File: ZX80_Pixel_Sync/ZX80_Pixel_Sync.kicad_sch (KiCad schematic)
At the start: 7 parts, among them IC202 74LS74, J1 IC201, J2 To_Minstrel2

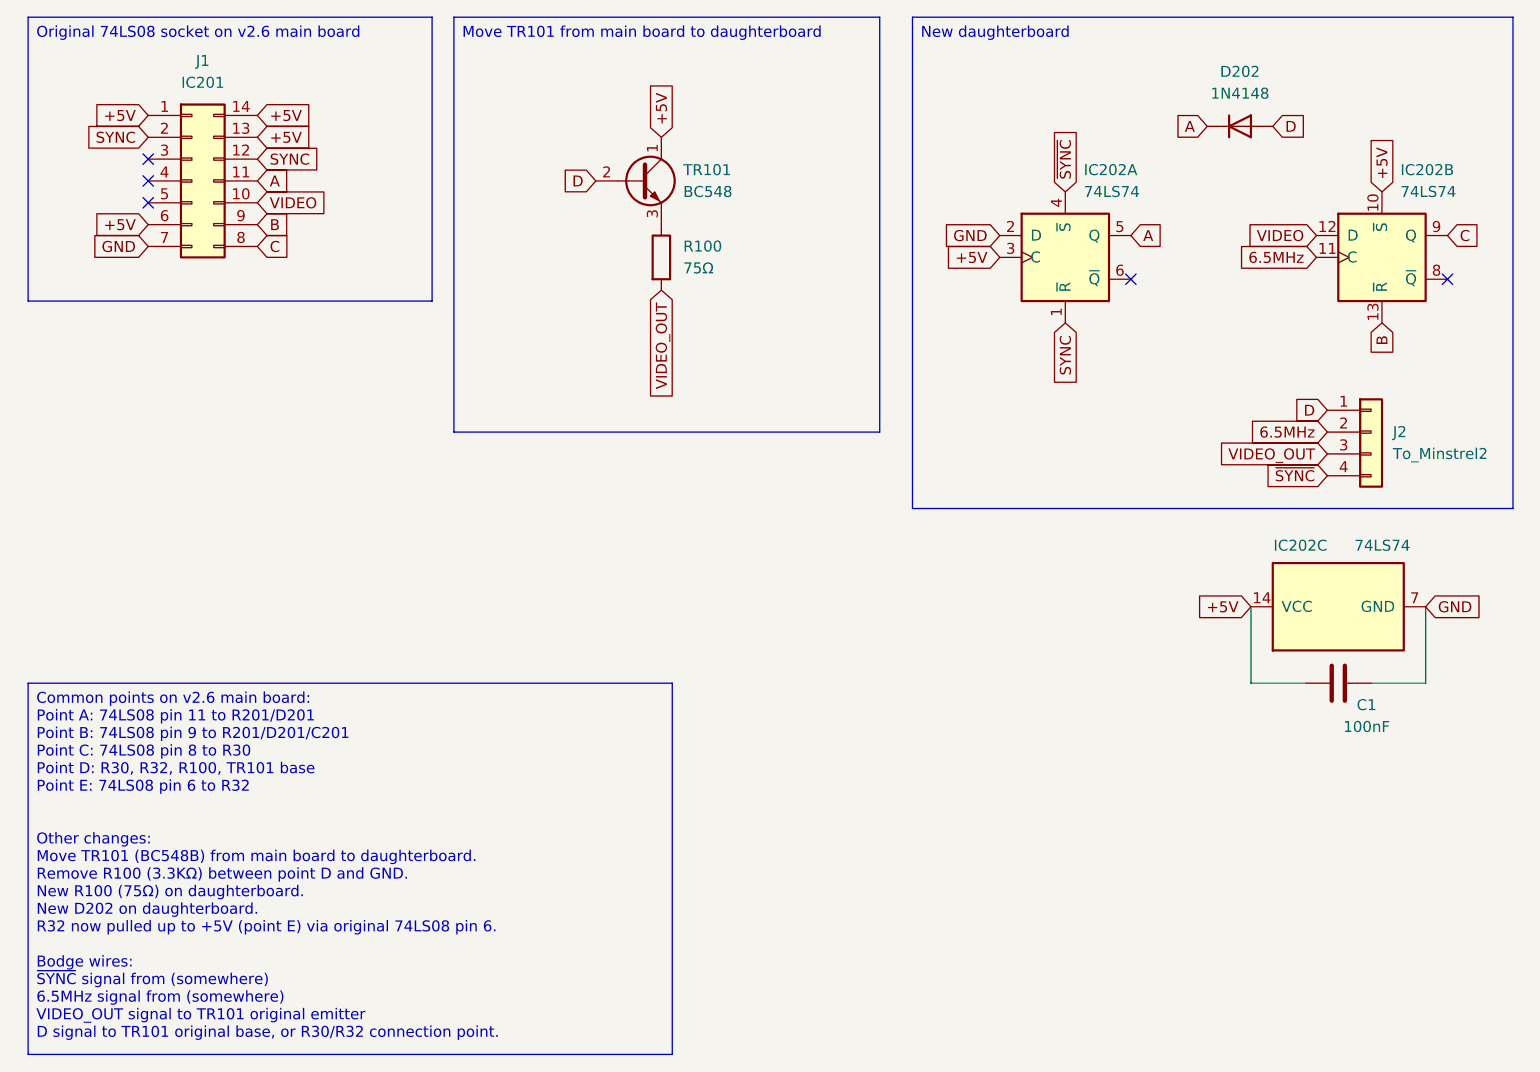
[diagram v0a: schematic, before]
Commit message: Modified PCB layout after testing initial layout
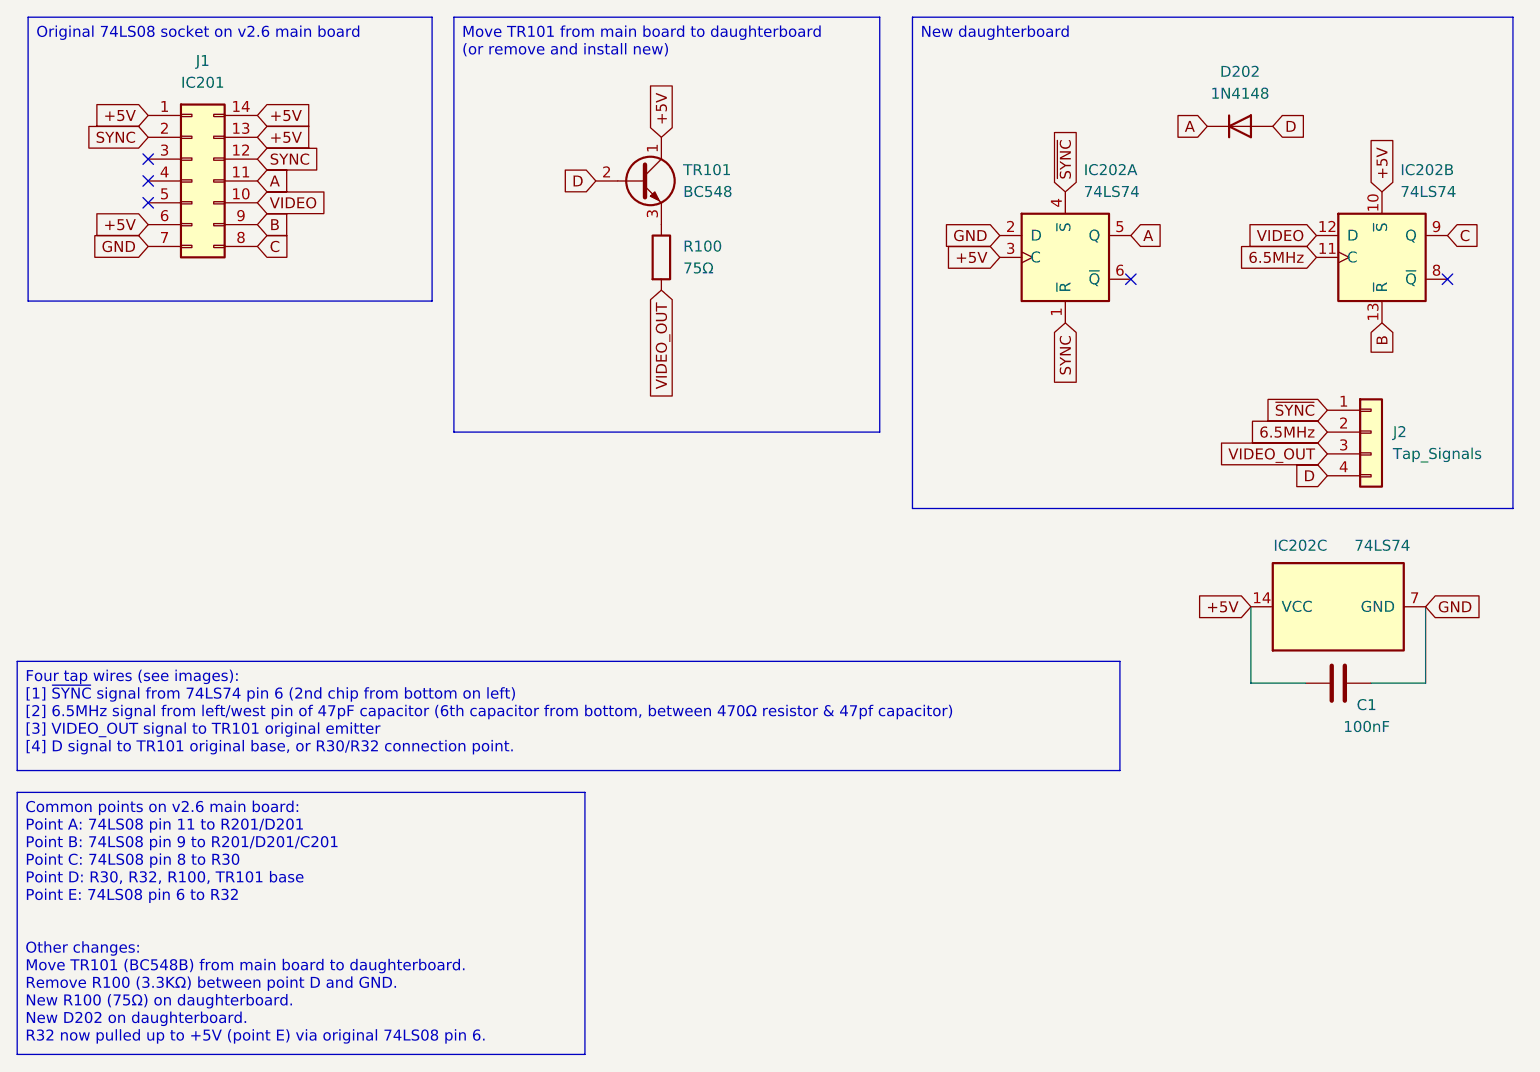
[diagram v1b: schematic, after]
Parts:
- J2: value To_Minstrel2 -> Tap_Signals
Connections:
- net D: now also J2.4 (Pin_4); no longer J2.1 (Pin_1)
- net ~{SYNC}: now also J2.1 (Pin_1); no longer J2.4 (Pin_4)
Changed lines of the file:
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@@
 		)
 	)
-	(text_box "Common points on v2.6 main board:\nPoint A: 74LS08 pin 11 to R201/D201\nPoint B: 74LS08 pin 9 to R201/D201/C201\nPoint C: 74LS08 pin 8 to R30\nPoint D: R30, R32, R100, TR101 base\nPoint E: 74LS08 pin 6 to R32\n\n\nOther changes:\nMove TR101 (BC548B) from main board to daughterboard.\nRemove R100 (3.3KΩ) between point D and GND.\nNew R100 (75Ω) on daughterboard.\nNew D202 on daughterboard.\nR32 now pulled up to +5V (point E) via original 74LS08 pin 6.\n\nBodge wires:\n~{SYNC} signal from (somewhere)\n6.5MHz signal from (somewhere)\nVIDEO_OUT signal to TR101 original emitter\nD signal to TR101 original base, or R30/R32 connection point."
+	(text_box "Common points on v2.6 main board:\nPoint A: 74LS08 pin 11 to R201/D201\nPoint B: 74LS08 pin 9 to R201/D201/C201\nPoint C: 74LS08 pin 8 to R30\nPoint D: R30, R32, R100, TR101 base\nPoint E: 74LS08 pin 6 to R32\n\n\nOther changes:\nMove TR101 (BC548B) from main board to daughterboard.\nRemove R100 (3.3KΩ) between point D and GND.\nNew R100 (75Ω) on daughterboard.\nNew D202 on daughterboard.\nR32 now pulled up to +5V (point E) via original 74LS08 pin 6.\n"
 		(exclude_from_sim no)
-		(at 13.97 91.44 0)
-		(size 74.93 43.18)
+		(at 12.7 104.14 0)
+		(size 66.04 30.48)
 		(margins 0.9525 0.9525 0.9525 0.9525)
 		(stroke
@@
 		)
 	)
-	(text_box "Move TR101 from main board to daughterboard"
+	(text_box "Move TR101 from main board to daughterboard\n(or remove and install new)"
 		(exclude_from_sim no)
 		(at 63.5 13.97 0)
@@
 		)
 	)
+	(text_box "Four tap wires (see images):\n[1] ~{SYNC} signal from 74LS74 pin 6 (2nd chip from bottom on left)\n[2] 6.5MHz signal from left/west pin of 47pF capacitor (6th capacitor from bottom, between 470Ω resistor & 47pf capacitor)\n[3] VIDEO_OUT signal to TR101 original emitter\n[4] D signal to TR101 original base, or R30/R32 connection point."
+		(exclude_from_sim no)
+		(at 12.7 88.9 0)
+		(size 128.27 12.7)
+		(margins 0.9525 0.9525 0.9525 0.9525)
+		(stroke
+			(width 0)
+			(type solid)
+		)
+		(fill
+			(type none)
+		)
+		(effects
+			(font
+				(size 1.27 1.27)
+			)
+			(justify left top)
+		)
+	)
 	(no_connect
 		(at 179.07 44.45)
@@
 		)
 	)
+	(global_label "6.5MHz"
+		(shape input)
+		(at 165.1 62.23 180)
+		(fields_autoplaced yes)
+		(effects
+			(font
+				(size 1.27 1.27)
+			)
+			(justify right)
+		)
+		(property "Intersheetrefs" "${INTERSHEET_REFS}"
+			(at 155.281 62.23 0)
+			(effects
+				(font
+					(size 1.27 1.27)
+				)
+				(justify right)
+				(hide yes)
+			)
+		)
+	)
 	(global_label "D"
 		(shape input)
+		(at 158.75 26.67 0)
+		(fields_autoplaced yes)
+		(effects
+			(font
+				(size 1.27 1.27)
+			)
+			(justify left)
+		)
+		(property "Intersheetrefs" "${INTERSHEET_REFS}"
+			(at 163.0052 26.67 0)
+			(effects
+				(font
+					(size 1.27 1.27)
+				)
+				(justify left)
+				(hide yes)
+			)
+		)
+	)
+	(global_label "+5V"
+		(shape input)
+		(at 27.94 38.1 180)
+		(fields_autoplaced yes)
+		(effects
+			(font
+				(size 1.27 1.27)
+			)
+			(justify right)
+		)
+		(property "Intersheetrefs" "${INTERSHEET_REFS}"
+			(at 21.0843 38.1 0)
+			(effects
+				(font
+					(size 1.27 1.27)
+				)
+				(justify right)
+				(hide yes)
+			)
+		)
+	)
+	(global_label "A"
+		(shape input)
+		(at 142.24 39.37 0)
+		(fields_autoplaced yes)
+		(effects
+			(font
+				(size 1.27 1.27)
+			)
+			(justify left)
+		)
+		(property "Intersheetrefs" "${INTERSHEET_REFS}"
+			(at 146.3138 39.37 0)
+			(effects
+				(font
+					(size 1.27 1.27)
+				)
+				(justify left)
+				(hide yes)
+			)
+		)
+	)
+	(global_label "6.5MHz"
+		(shape input)
+		(at 163.83 41.91 180)
+		(fields_autoplaced yes)
+		(effects
+			(font
+				(size 1.27 1.27)
+			)
+			(justify right)
+		)
+		(property "Intersheetrefs" "${INTERSHEET_REFS}"
+			(at 154.011 41.91 0)
+			(effects
+				(font
+					(size 1.27 1.27)
+				)
+				(justify right)
+				(hide yes)
+			)
+		)
+	)
+	(global_label "+5V"
+		(shape input)
+		(at 171.45 34.29 90)
+		(fields_autoplaced yes)
+		(effects
+			(font
+				(size 1.27 1.27)
+			)
+			(justify left)
+		)
+		(property "Intersheetrefs" "${INTERSHEET_REFS}"
+			(at 171.45 27.4343 90)
+			(effects
+				(font
+					(size 1.27 1.27)
+				)
+				(justify left)
+				(hide yes)
+			)
+		)
+	)
+	(global_label "~{SYNC}"
+		(shape input)
 		(at 165.1 59.69 180)
 		(fields_autoplaced yes)
@@
 		)
 		(property "Intersheetrefs" "${INTERSHEET_REFS}"
-			(at 160.8448 59.69 0)
-			(effects
-				(font
-					(size 1.27 1.27)
-				)
-				(justify right)
-				(hide yes)
-			)
-		)
-	)
-	(global_label "6.5MHz"
-		(shape input)
-		(at 165.1 62.23 180)
-		(fields_autoplaced yes)
-		(effects
-			(font
-				(size 1.27 1.27)
-			)
-			(justify right)
-		)
-		(property "Intersheetrefs" "${INTERSHEET_REFS}"
-			(at 155.281 62.23 0)
-			(effects
-				(font
-					(size 1.27 1.27)
-				)
-				(justify right)
+			(at 157.2162 59.69 0)
+			(effects
+				(font
+					(size 1.27 1.27)
+				)
+				(justify right)
+				(hide yes)
+			)
+		)
+	)
+	(global_label "GND"
+		(shape input)
+		(at 176.53 82.55 0)
+		(fields_autoplaced yes)
+		(effects
+			(font
+				(size 1.27 1.27)
+			)
+			(justify left)
+		)
+		(property "Intersheetrefs" "${INTERSHEET_REFS}"
+			(at 183.3857 82.55 0)
+			(effects
+				(font
+					(size 1.27 1.27)
+				)
+				(justify left)
+				(hide yes)
+			)
+		)
+	)
+	(global_label "~{SYNC}"
+		(shape input)
+		(at 134.62 34.29 90)
+		(fields_autoplaced yes)
+		(effects
+			(font
+				(size 1.27 1.27)
+			)
+			(justify left)
+		)
+		(property "Intersheetrefs" "${INTERSHEET_REFS}"
+			(at 134.62 26.4062 90)
+			(effects
+				(font
+					(size 1.27 1.27)
+				)
+				(justify left)
 				(hide yes)
 			)
@@
 	(global_label "D"
 		(shape input)
-		(at 158.75 26.67 0)
-		(fields_autoplaced yes)
-		(effects
-			(font
-				(size 1.27 1.27)
-			)
-			(justify left)
-		)
-		(property "Intersheetrefs" "${INTERSHEET_REFS}"
-			(at 163.0052 26.67 0)
-			(effects
-				(font
-					(size 1.27 1.27)
-				)
-				(justify left)
-				(hide yes)
-			)
-		)
-	)
-	(global_label "+5V"
-		(shape input)
-		(at 27.94 38.1 180)
-		(fields_autoplaced yes)
-		(effects
-			(font
-				(size 1.27 1.27)
-			)
-			(justify right)
-		)
-		(property "Intersheetrefs" "${INTERSHEET_REFS}"
-			(at 21.0843 38.1 0)
-			(effects
-				(font
-					(size 1.27 1.27)
-				)
-				(justify right)
-				(hide yes)
-			)
-		)
-	)
-	(global_label "~{SYNC}"
-		(shape input)
 		(at 165.1 67.31 180)
 		(fields_autoplaced yes)
@@
 		)
 		(property "Intersheetrefs" "${INTERSHEET_REFS}"
-			(at 157.2162 67.31 0)
-			(effects
-				(font
-					(size 1.27 1.27)
-				)
-				(justify right)
-				(hide yes)
-			)
-		)
-	)
-	(global_label "A"
-		(shape input)
-		(at 142.24 39.37 0)
-		(fields_autoplaced yes)
-		(effects
-			(font
-				(size 1.27 1.27)
-			)
-			(justify left)
-		)
-		(property "Intersheetrefs" "${INTERSHEET_REFS}"
-			(at 146.3138 39.37 0)
-			(effects
-				(font
-					(size 1.27 1.27)
-				)
-				(justify left)
-				(hide yes)
-			)
-		)
-	)
-	(global_label "6.5MHz"
-		(shape input)
-		(at 163.83 41.91 180)
-		(fields_autoplaced yes)
-		(effects
-			(font
-				(size 1.27 1.27)
-			)
-			(justify right)
-		)
-		(property "Intersheetrefs" "${INTERSHEET_REFS}"
-			(at 154.011 41.91 0)
-			(effects
-				(font
-					(size 1.27 1.27)
-				)
-				(justify right)
-				(hide yes)
-			)
-		)
-	)
-	(global_label "+5V"
-		(shape input)
-		(at 171.45 34.29 90)
-		(fields_autoplaced yes)
-		(effects
-			(font
-				(size 1.27 1.27)
-			)
-			(justify left)
-		)
-		(property "Intersheetrefs" "${INTERSHEET_REFS}"
-			(at 171.45 27.4343 90)
-			(effects
-				(font
-					(size 1.27 1.27)
-				)
-				(justify left)
-				(hide yes)
-			)
-		)
-	)
-	(global_label "GND"
-		(shape input)
-		(at 176.53 82.55 0)
-		(fields_autoplaced yes)
-		(effects
-			(font
-				(size 1.27 1.27)
-			)
-			(justify left)
-		)
-		(property "Intersheetrefs" "${INTERSHEET_REFS}"
-			(at 183.3857 82.55 0)
-			(effects
-				(font
-					(size 1.27 1.27)
-				)
-				(justify left)
-				(hide yes)
-			)
-		)
-	)
-	(global_label "~{SYNC}"
-		(shape input)
-		(at 134.62 34.29 90)
-		(fields_autoplaced yes)
-		(effects
-			(font
-				(size 1.27 1.27)
-			)
-			(justify left)
-		)
-		(property "Intersheetrefs" "${INTERSHEET_REFS}"
-			(at 134.62 26.4062 90)
-			(effects
-				(font
-					(size 1.27 1.27)
-				)
-				(justify left)
+			(at 160.8448 67.31 0)
+			(effects
+				(font
+					(size 1.27 1.27)
+				)
+				(justify right)
 				(hide yes)
 			)
@@
 			)
 		)
-		(property "Value" "To_Minstrel2"
+		(property "Value" "Tap_Signals"
 			(at 172.72 64.7699 0)
 			(effects
